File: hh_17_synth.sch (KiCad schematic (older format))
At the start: 22 parts

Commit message: switch to 48 pin chip, add headphone jack etc.
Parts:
- removed C?: 100nF, symbol C_Small
- removed U?: STM32F072RxTx, LQFP64, symbol STM32F072RxTx
- added C5, C6: 1uF, symbol C
- added C7, C8: 0.1uF, symbol C
- added J3: JACK_TRS, custom:Tayda_3.5mm_stereo_TRS_jack_A-853, symbol JACK_TRS
- added R2, R3: 8, symbol R
- added U2: STM32F072CBTx, Housings_QFP:LQFP-48_7x7mm_Pitch0.5mm, symbol STM32F072CBTx
- J1: renamed from J?; footprint (none) -> custom:HDMI_476420001_CONN
- J2: renamed from J?; footprint (none) -> Pin_Headers:Pin_Header_Straight_1x05_Pitch2.54mm
- SW1: renamed from SW?; footprint (none) -> Buttons_Switches_ThroughHole:SW_PUSH_6mm
- U1: renamed from U?; footprint (none) -> TO_SOT_Packages_SMD:SOT-223
- gave numbers to parts that had none: 16
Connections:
- wire segments 84 -> 97
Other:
- note added: "http://www.taydaelectronics.com/review/product/list/id/2876/"
- moved on the sheet: C1, C10, C12, C13, C14, C15, C16, C17, C18, C2, C3, C4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

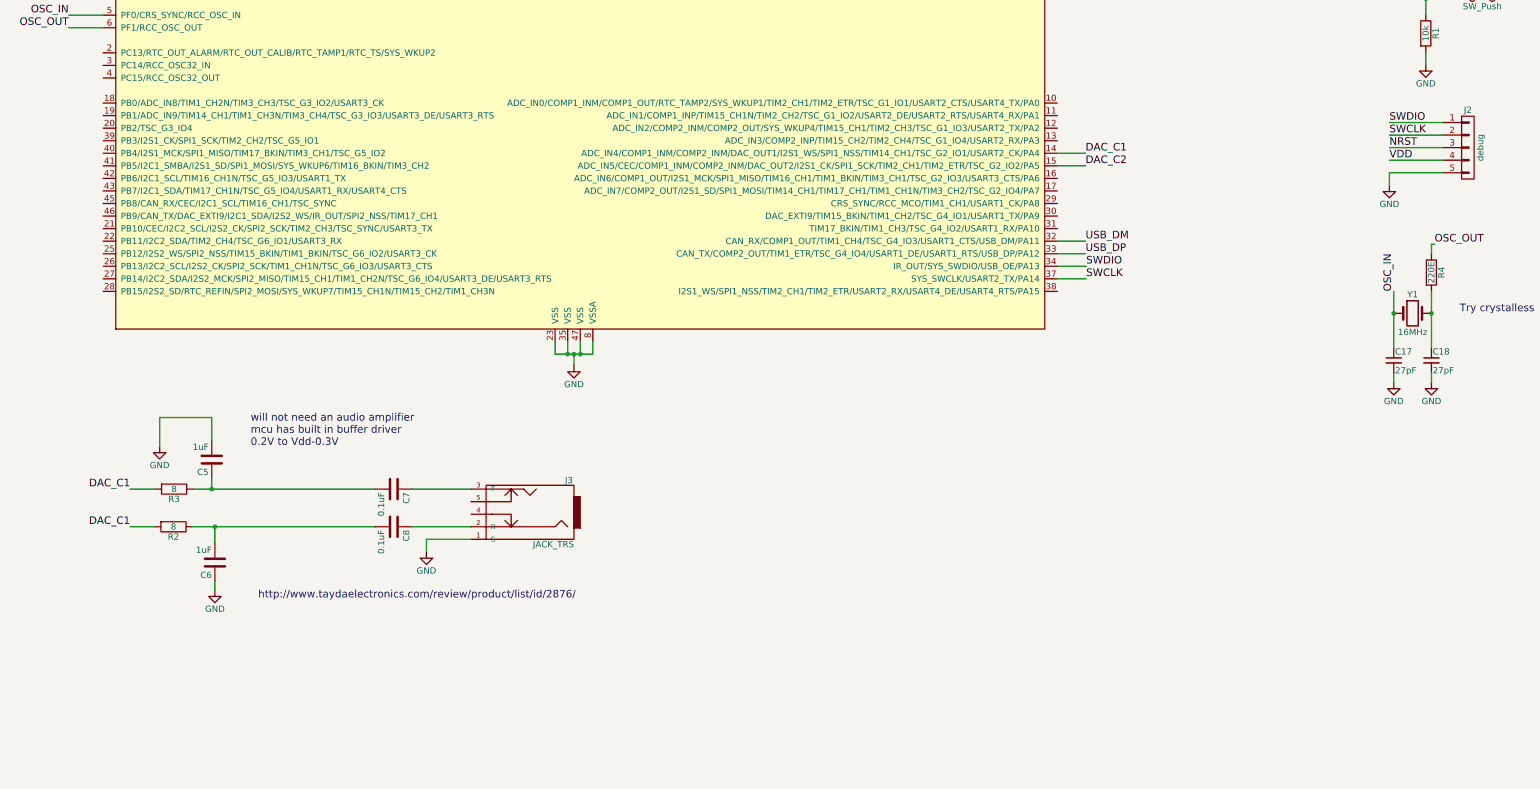
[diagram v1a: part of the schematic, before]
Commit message: Imported Mitch's touchpad and keyboard lib/mod
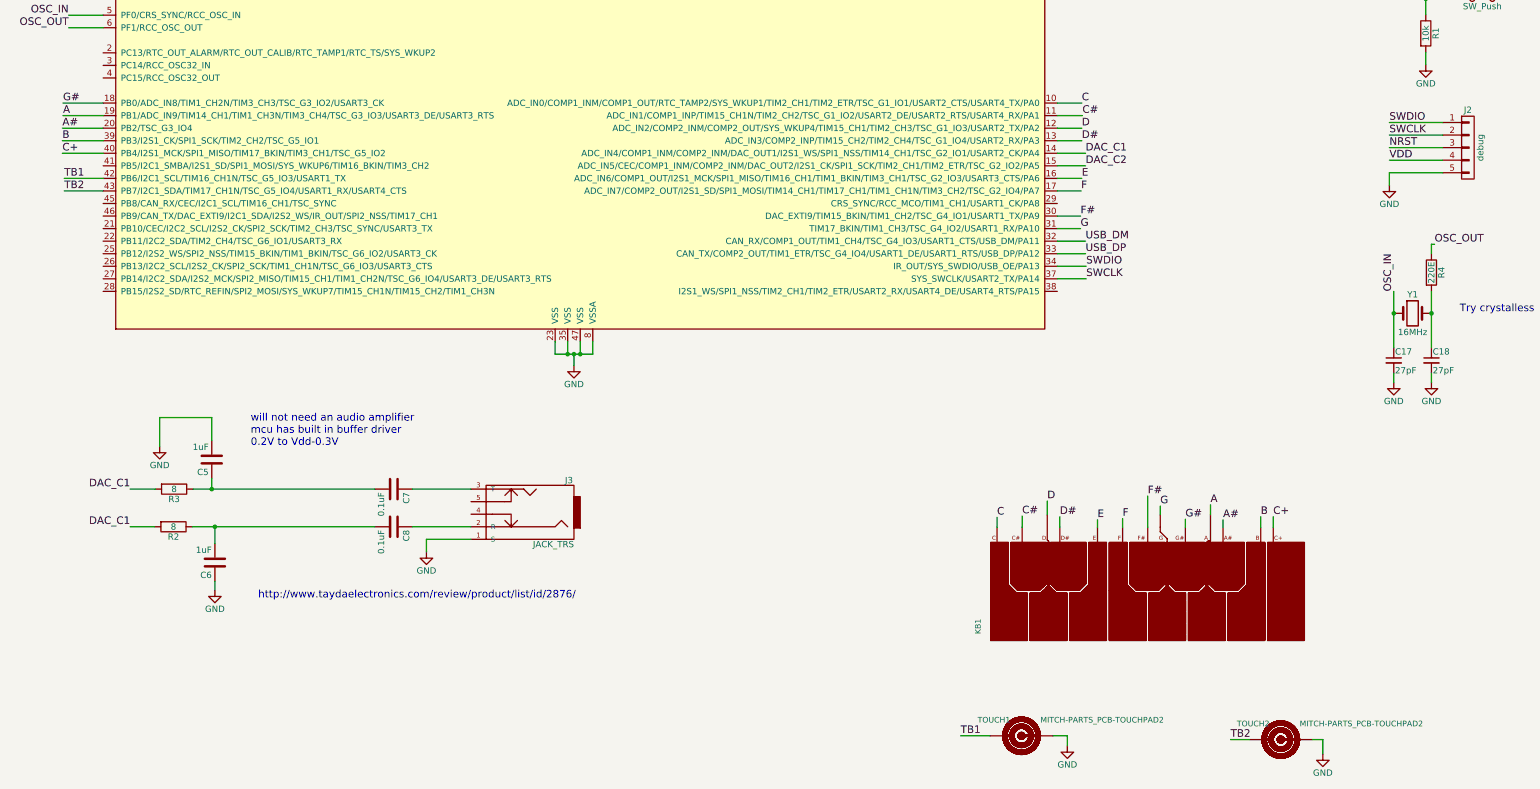
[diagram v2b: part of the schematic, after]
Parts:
- added KB1: MITCH-PARTS_PCB-KEYBOARD2, custom:MITCH-PARTS_PCB-KEYBOARD2_kicad_fix, symbol MITCH-PARTS_PCB-KEYBOARD2
- added TOUCH1, TOUCH2: MITCH-PARTS_PCB-TOUCHPAD2, custom:MITCH-PARTS_PCB-TOUCHPAD2_kicad_fix, symbol MITCH-PARTS_PCB-TOUCHPAD2
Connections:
- net GND: now also TOUCH1.2, TOUCH2.2
- net C: now reaches U2.10 (ADC_IN0/COMP1_INM/COMP1_OUT/RTC_TAMP2/SYS_WKUP1/TIM2_CH1/TIM2_ETR/TSC_G1_IO1/USART2_CTS/USART4_TX/PA0)
- net C: now also KB1.C
- net C#: now reaches U2.11 (ADC_IN1/COMP1_INP/TIM15_CH1N/TIM2_CH2/TSC_G1_IO2/USART2_DE/USART2_RTS/USART4_RX/PA1)
- net C#: now also KB1.C#
- net D: now reaches U2.12 (ADC_IN2/COMP2_INM/COMP2_OUT/SYS_WKUP4/TIM15_CH1/TIM2_CH3/TSC_G1_IO3/USART2_TX/PA2)
- net D: now also KB1.D
- net D#: now reaches U2.13 (ADC_IN3/COMP2_INP/TIM15_CH2/TIM2_CH4/TSC_G1_IO4/USART2_RX/PA3)
- net D#: now also KB1.D#
- net E: now reaches U2.16 (ADC_IN6/COMP1_OUT/I2S1_MCK/SPI1_MISO/TIM16_CH1/TIM1_BKIN/TIM3_CH1/TSC_G2_IO3/USART3_CTS/PA6)
- net E: now also KB1.E
- net F: now reaches U2.17 (ADC_IN7/COMP2_OUT/I2S1_SD/SPI1_MOSI/TIM14_CH1/TIM17_CH1/TIM1_CH1N/TIM3_CH2/TSC_G2_IO4/PA7)
- net F: now also KB1.F
- net G#: now reaches U2.18 (PB0/ADC_IN8/TIM1_CH2N/TIM3_CH3/TSC_G3_IO2/USART3_CK)
- net G#: now also KB1.G#
- net A: now reaches U2.19 (PB1/ADC_IN9/TIM14_CH1/TIM1_CH3N/TIM3_CH4/TSC_G3_IO3/USART3_DE/USART3_RTS)
- net A: now also KB1.A
- net A#: now reaches U2.20 (PB2/TSC_G3_IO4)
- net A#: now also KB1.A#
- net F#: now reaches U2.30 (DAC_EXTI9/TIM15_BKIN/TIM1_CH2/TSC_G4_IO1/USART1_TX/PA9)
- net F#: now also KB1.F#
- net G: now reaches U2.31 (TIM17_BKIN/TIM1_CH3/TSC_G4_IO2/USART1_RX/PA10)
- net G: now also KB1.G
- net B: now reaches U2.39 (PB3/I2S1_CK/SPI1_SCK/TIM2_CH2/TSC_G5_IO1)
- net B: now also KB1.B
- net C+: now reaches U2.40 (PB4/I2S1_MCK/SPI1_MISO/TIM17_BKIN/TIM3_CH1/TSC_G5_IO2)
- net C+: now also KB1.C+
- net TB1: now reaches U2.42 (PB6/I2C1_SCL/TIM16_CH1N/TSC_G5_IO3/USART1_TX)
- net TB1: now also TOUCH1.1
- net TB2: now reaches U2.43 (PB7/I2C1_SDA/TIM17_CH1N/TSC_G5_IO4/USART1_RX/USART4_CTS)
- net TB2: now also TOUCH2.1
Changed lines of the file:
@@
 LIBS:zetex
 LIBS:JACK_TRS
+LIBS:ArduTouch_stereo_v1.2
+LIBS:mitch_exported
 LIBS:hh_17_synth-cache
 EELAYER 25 0
@@
 Wire Wire Line
 	11715 5185 11485 5185
+$Comp
+L MITCH-PARTS_PCB-KEYBOARD2 KB1
+U 1 1 58A88168
+P 12205 7665
+F 0 "KB1" V 10880 7315 45  0000 L BNN
+F 1 "MITCH-PARTS_PCB-KEYBOARD2" V 12205 7665 45  0001 L BNN
+F 2 "custom:MITCH-PARTS_PCB-KEYBOARD2_kicad_fix" H 12235 7815 20  0001 C CNN
+F 3 "" H 12205 7665 60  0001 C CNN
+	1    12205 7665
+	1    0    0    -1
+$EndComp
+$Comp
+L MITCH-PARTS_PCB-TOUCHPAD2 TOUCH1
+U 1 1 58A8CBB1
+P 11200 8825
+F 0 "TOUCH1" H 10850 8925 45  0000 L BNN
+F 1 "MITCH-PARTS_PCB-TOUCHPAD2" H 11350 8925 45  0000 L BNN
+F 2 "custom:MITCH-PARTS_PCB-TOUCHPAD2_kicad_fix" H 11230 8975 20  0001 C CNN
+F 3 "" H 11200 8825 60  0001 C CNN
+	1    11200 8825
+	1    0    0    -1
+$EndComp
+$Comp
+L MITCH-PARTS_PCB-TOUCHPAD2 TOUCH2
+U 1 1 58A8CCDE
+P 13265 8855
+F 0 "TOUCH2" H 12915 8955 45  0000 L BNN
+F 1 "MITCH-PARTS_PCB-TOUCHPAD2" H 13415 8955 45  0000 L BNN
+F 2 "custom:MITCH-PARTS_PCB-TOUCHPAD2_kicad_fix" H 13295 9005 20  0001 C CNN
+F 3 "" H 13265 8855 60  0001 C CNN
+	1    13265 8855
+	1    0    0    -1
+$EndComp
+Text Label 11680 3785 0    60   ~ 0
+C
+Text Label 11685 3885 0    60   ~ 0
+C#
+Text Label 11680 3985 0    60   ~ 0
+D
+Text Label 11680 4085 0    60   ~ 0
+D#
+Wire Wire Line
+	11485 4085 11680 4085
+Wire Wire Line
+	11680 3985 11485 3985
+Wire Wire Line
+	11485 3885 11685 3885
+Wire Wire Line
+	11680 3785 11485 3785
+Text Label 11005 7085 0    60   ~ 0
+C
+Wire Wire Line
+	11005 7085 11005 7165
+Text Label 11205 7075 0    60   ~ 0
+C#
+Wire Wire Line
+	11205 7075 11205 7165
+Text Label 11405 6955 0    60   ~ 0
+D
+Wire Wire Line
+	11405 6955 11405 7065
+Text Label 11505 7080 0    60   ~ 0
+D#
+Wire Wire Line
+	11505 7080 11505 7165
+Text Label 11680 4385 0    60   ~ 0
+E
+Text Label 11675 4485 0    60   ~ 0
+F
+Wire Wire Line
+	11675 4485 11485 4485
+Wire Wire Line
+	11680 4385 11485 4385
+Text Label 11805 7105 0    60   ~ 0
+E
+Wire Wire Line
+	11805 7105 11805 7165
+Text Label 12005 7095 0    60   ~ 0
+F
+Wire Wire Line
+	12005 7095 12005 7165
+Text Label 11670 4685 0    60   ~ 0
+F#
+Wire Wire Line
+	11670 4685 11485 4685
+Text Label 11670 4785 0    60   ~ 0
+G
+Wire Wire Line
+	11670 4785 11485 4785
+Text Label 12205 6915 0    60   ~ 0
+F#
+Wire Wire Line
+	12205 6915 12205 7165
+Text Label 12305 6995 0    60   ~ 0
+G
+Wire Wire Line
+	12305 6995 12305 7065
+Text Label 3565 3785 0    60   ~ 0
+G#
+Text Label 3565 3885 0    60   ~ 0
+A
+Text Label 3560 3985 0    60   ~ 0
+A#
+Wire Wire Line
+	3560 3985 3885 3985
+Wire Wire Line
+	3885 3885 3565 3885
+Wire Wire Line
+	3565 3785 3885 3785
+Text Label 12505 7100 0    60   ~ 0
+G#
+Wire Wire Line
+	12505 7100 12505 7165
+Text Label 12705 6985 0    60   ~ 0
+A
+Wire Wire Line
+	12705 6985 12705 7065
+Text Label 12805 7105 0    60   ~ 0
+A#
+Wire Wire Line
+	12805 7105 12805 7165
+Text Label 13105 7080 0    60   ~ 0
+B
+Text Label 13205 7080 0    60   ~ 0
+C+
+Wire Wire Line
+	13105 7080 13105 7165
+Wire Wire Line
+	13205 7165 13205 7080
+Text Label 3560 4085 0    60   ~ 0
+B
+Text Label 3560 4185 0    60   ~ 0
+C+
+Wire Wire Line
+	3560 4185 3885 4185
+Wire Wire Line
+	3885 4085 3560 4085
+$Comp
+L GND #PWR015
+U 1 1 58A9B332
+P 11565 8905
+F 0 "#PWR015" H 11565 8655 50  0001 C CNN
+F 1 "GND" H 11565 8755 50  0000 C CNN
+F 2 "" H 11565 8905 50  0001 C CNN
+F 3 "" H 11565 8905 50  0001 C CNN
+	1    11565 8905
+	1    0    0    -1
+$EndComp
+Wire Wire Line
+	11450 8825 11565 8825
+Wire Wire Line
+	11565 8825 11565 8905
+$Comp
+L GND #PWR016
+U 1 1 58A9B570
+P 13600 8970
+F 0 "#PWR016" H 13600 8720 50  0001 C CNN
+F 1 "GND" H 13600 8820 50  0000 C CNN
+F 2 "" H 13600 8970 50  0001 C CNN
+F 3 "" H 13600 8970 50  0001 C CNN
+	1    13600 8970
+	1    0    0    -1
+$EndComp
+Wire Wire Line
+	13600 8970 13600 8855
+Wire Wire Line
+	13600 8855 13515 8855
+Text Label 3575 4385 0    60   ~ 0
+TB1
+Text Label 3575 4485 0    60   ~ 0
+TB2
+Wire Wire Line
+	3575 4485 3885 4485
+Wire Wire Line
+	3575 4385 3885 4385
+Text Label 10715 8825 0    60   ~ 0
+TB1
+Wire Wire Line
+	10715 8825 10950 8825
+Text Label 12865 8855 0    60   ~ 0
+TB2
+Wire Wire Line
+	13015 8855 12865 8855
 $EndSCHEMATC

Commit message: placed parts, changed some footprints.
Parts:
- removed C6: 1uF, symbol C
- added C6: 1uF, Capacitors_ThroughHole:CP_Radial_D5.0mm_P2.00mm, symbol CP1
- C1: value C -> 1uF; footprint (none) -> Capacitors_SMD:C_0603
- C10, C12, C13, C14, C15, C16, C17, C18, C2, C3, C4, C7, C8, C9: footprint (none) -> Capacitors_SMD:C_0603
- C5: footprint (none) -> Capacitors_ThroughHole:CP_Radial_D5.0mm_P2.00mm; symbol C -> CP1; Manufacturer (none) -> Cornell Dubilier; Mfg_Part_No (none) -> 105CKR050M
- R1, R2, R3, R4: footprint (none) -> Resistors_SMD:R_0603
- Y1: footprint (none) -> Crystals:Crystal_HC49-4H_Vertical
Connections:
- net DAC_C1: no longer R2.2
- net DAC_C2: now also R2.2
- net GND: now also C6.2
- net at C8.2, R2.1: now also C6.1
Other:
- note added: "TODO: choose button and verify button footprint"
- note added: "TODO: verify load capacitance, fix crystal"
- note added: "TODO: verify lpf"
- note removed: "Try crystalless"
- moved on the sheet: R2, R3
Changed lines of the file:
@@
 LIBS:JACK_TRS
 LIBS:ArduTouch_stereo_v1.2
-LIBS:mitch_exported
 LIBS:hh_17_synth-cache
 EELAYER 25 0
@@
 F 0 "Y1" H 14315 5610 50  0000 C CNN
 F 1 "16MHz" H 14315 5310 50  0000 C CNN
-F 2 "" H 14315 5460 50  0001 C CNN
+F 2 "Crystals:Crystal_HC49-4H_Vertical" H 14315 5460 50  0001 C CNN
 F 3 "" H 14315 5460 50  0000 C CNN
 	1    14315 5460
@@
 F 0 "R4" V 14545 5135 50  0000 C CNN
 F 1 "220E" V 14465 5135 50  0000 C CNN
-F 2 "" V 14395 5135 50  0001 C CNN
+F 2 "Resistors_SMD:R_0603" V 14395 5135 50  0001 C CNN
 F 3 "" H 14465 5135 50  0000 C CNN
 	1    14465 5135
@@
 F 0 "C17" H 14175 5905 50  0000 L CNN
 F 1 "27pF" H 14175 5755 50  0000 L CNN
-F 2 "" H 14165 5835 50  0001 C CNN
+F 2 "Capacitors_SMD:C_0603" H 14165 5835 50  0001 C CNN
 F 3 "" H 14165 5835 50  0000 C CNN
 	1    14165 5835
@@
 F 0 "C18" H 14475 5905 50  0000 L CNN
 F 1 "27pF" H 14475 5755 50  0000 L CNN
-F 2 "" H 14465 5835 50  0001 C CNN
+F 2 "Capacitors_SMD:C_0603" H 14465 5835 50  0001 C CNN
 F 3 "" H 14465 5835 50  0000 C CNN
 	1    14465 5835
@@
 F 0 "C12" H 7865 1220 50  0000 L CNN
 F 1 "100nF" V 7855 750 50  0000 L CNN
-F 2 "" H 7855 1150 50  0001 C CNN
+F 2 "Capacitors_SMD:C_0603" H 7855 1150 50  0001 C CNN
 F 3 "" H 7855 1150 50  0000 C CNN
 	1    7855 1150
@@
 F 0 "C13" H 7865 1395 50  0000 L CNN
 F 1 "100nF" V 7855 925 50  0000 L CNN
-F 2 "" H 7855 1325 50  0001 C CNN
+F 2 "Capacitors_SMD:C_0603" H 7855 1325 50  0001 C CNN
 F 3 "" H 7855 1325 50  0000 C CNN
 	1    7855 1325
@@
 F 0 "C14" H 7865 1570 50  0000 L CNN
 F 1 "4.7uF" V 7855 1100 50  0000 L CNN
-F 2 "" H 7855 1500 50  0001 C CNN
+F 2 "Capacitors_SMD:C_0603" H 7855 1500 50  0001 C CNN
 F 3 "" H 7855 1500 50  0000 C CNN
 	1    7855 1500
@@
 F 0 "C16" H 8490 1570 50  0000 L CNN
 F 1 "10nF" V 8480 1100 50  0000 L CNN
-F 2 "" H 8480 1500 50  0001 C CNN
+F 2 "Capacitors_SMD:C_0603" H 8480 1500 50  0001 C CNN
 F 3 "" H 8480 1500 50  0000 C CNN
 	1    8480 1500
@@
 F 0 "C15" H 8490 1395 50  0000 L CNN
 F 1 "1uF" V 8480 925 50  0000 L CNN
-F 2 "" H 8480 1325 50  0001 C CNN
+F 2 "Capacitors_SMD:C_0603" H 8480 1325 50  0001 C CNN
 F 3 "" H 8480 1325 50  0000 C CNN
 	1    8480 1325
@@
 F 0 "C9" H 9200 1740 50  0000 L CNN
 F 1 "100nF" V 9240 1370 50  0000 L CNN
-F 2 "" H 9190 1670 50  0001 C CNN
+F 2 "Capacitors_SMD:C_0603" H 9190 1670 50  0001 C CNN
 F 3 "" H 9190 1670 50  0000 C CNN
 	1    9190 1670
@@
 F 0 "C10" H 9200 1940 50  0000 L CNN
 F 1 "4.7uF" V 9240 1595 50  0000 L CNN
-F 2 "" H 9190 1870 50  0001 C CNN
+F 2 "Capacitors_SMD:C_0603" H 9190 1870 50  0001 C CNN
 F 3 "" H 9190 1870 50  0000 C CNN
 	1    9190 1870
@@
 F 0 "C2" V 13115 790 50  0000 L CNN
 F 1 "1uF" V 13065 1165 50  0000 L CNN
-F 2 "" H 13065 940 50  0001 C CNN
+F 2 "Capacitors_SMD:C_0603" H 13065 940 50  0001 C CNN
 F 3 "" H 13065 940 50  0000 C CNN
 	1    13065 940
@@
 F 0 "C3" V 13115 965 50  0000 L CNN
 F 1 "100nF" V 13015 1340 50  0000 L CNN
-F 2 "" H 13065 1115 50  0001 C CNN
+F 2 "Capacitors_SMD:C_0603" H 13065 1115 50  0001 C CNN
 F 3 "" H 13065 1115 50  0000 C CNN
 	1    13065 1115
@@
 F 0 "C4" V 13115 1140 50  0000 L CNN
 F 1 "10nF" V 13065 1515 50  0000 L CNN
-F 2 "" H 13065 1290 50  0001 C CNN
+F 2 "Capacitors_SMD:C_0603" H 13065 1290 50  0001 C CNN
 F 3 "" H 13065 1290 50  0000 C CNN
 	1    13065 1290
@@
 Text Label 11710 4985 0    60   ~ 0
 USB_DP
-Text Notes 14690 5460 0    60   ~ 0
-Try crystalless
 $Comp
 L LM1117-3.3 U1
@@
 P 15145 1650
 F 0 "C1" H 15170 1750 50  0000 L CNN
-F 1 "C" H 15170 1550 50  0000 L CNN
-F 2 "" H 15183 1500 50  0001 C CNN
+F 1 "1uF" H 15170 1550 50  0000 L CNN
+F 2 "Capacitors_SMD:C_0603" H 15183 1500 50  0001 C CNN
 F 3 "" H 15145 1650 50  0001 C CNN
 	1    15145 1650
@@
 F 0 "R1" V 14500 3230 50  0000 C CNN
 F 1 "10k" V 14420 3230 50  0000 C CNN
-F 2 "" V 14350 3230 50  0001 C CNN
+F 2 "Resistors_SMD:R_0603" V 14350 3230 50  0001 C CNN
 F 3 "" H 14420 3230 50  0001 C CNN
 	1    14420 3230
@@
 	-1   0    0    1
 $EndComp
-Text Notes 5120 7740 0    60   ~ 0
+Text Notes 5790 8090 0    60   ~ 0
 http://www.taydaelectronics.com/review/product/list/id/2876/
 $Comp
@@
 	1    0    0    -1
 $EndComp
-Text Label 4100 7160 2    60   ~ 0
-DAC_C1
-Text Label 4100 6860 2    60   ~ 0
+Text Label 3530 7535 2    60   ~ 0
+DAC_C2
+Text Label 3555 6860 2    60   ~ 0
 DAC_C1
 $Comp
@@
 F 0 "C8" H 6225 7260 50  0000 L CNN
 F 1 "0.1uF" H 6225 7060 50  0000 L CNN
-F 2 "" H 6238 7010 50  0001 C CNN
+F 2 "Capacitors_SMD:C_0603" H 6238 7010 50  0001 C CNN
 F 3 "" H 6200 7160 50  0001 C CNN
 	1    6200 7160
@@
 F 0 "C7" H 6225 6960 50  0000 L CNN
 F 1 "0.1uF" H 6225 6760 50  0000 L CNN
-F 2 "" H 6238 6710 50  0001 C CNN
+F 2 "Capacitors_SMD:C_0603" H 6238 6710 50  0001 C CNN
 F 3 "" H 6200 6860 50  0001 C CNN
 	1    6200 6860
@@
 $EndComp
 $Comp
-L C C5
+L CP1 C5
 U 1 1 58A72315
-P 4750 6625
-F 0 "C5" H 4775 6725 50  0000 L CNN
-F 1 "1uF" H 4775 6525 50  0000 L CNN
-F 2 "" H 4788 6475 50  0001 C CNN
-F 3 "" H 4750 6625 50  0001 C CNN
-	1    4750 6625
-	-1   0    0    1
-$EndComp
-$Comp
-L C C6
-U 1 1 58A7240F
-P 4775 7445
-F 0 "C6" H 4800 7545 50  0000 L CNN
-F 1 "1uF" H 4800 7345 50  0000 L CNN
-F 2 "" H 4813 7295 50  0001 C CNN
-F 3 "" H 4775 7445 50  0001 C CNN
-	1    4775 7445
-	-1   0    0    1
+P 4205 7095
+F 0 "C5" H 4230 7195 50  0000 L CNN
+F 1 "1uF" H 4230 6995 50  0000 L CNN
+F 2 "Capacitors_ThroughHole:CP_Radial_D5.0mm_P2.00mm" H 4243 6945 50  0001 C CNN
+F 3 "" H 4205 7095 50  0001 C CNN
+F 4 "105CKR050M" H 4205 7095 60  0001 C CNN "Mfg_Part_No"
+F 5 "Cornell Dubilier" H 4205 7095 60  0001 C CNN "Manufacturer"
+	1    4205 7095
+	1    0    0    -1
 $EndComp
 $Comp
 L GND #PWR012
 U 1 1 58A724D3
-P 4335 6520
-F 0 "#PWR012" H 4335 6270 50  0001 C CNN
-F 1 "GND" H 4335 6370 50  0000 C CNN
-F 2 "" H 4335 6520 50  0001 C CNN
-F 3 "" H 4335 6520 50  0001 C CNN
-	1    4335 6520
+P 4205 7320
+F 0 "#PWR012" H 4205 7070 50  0001 C CNN
+F 1 "GND" H 4205 7170 50  0000 C CNN
+F 2 "" H 4205 7320 50  0001 C CNN
+F 3 "" H 4205 7320 50  0001 C CNN
+	1    4205 7320
 	1    0    0    -1
 $EndComp
@@
 L GND #PWR013
 U 1 1 58A72C41
-P 4775 7665
-F 0 "#PWR013" H 4775 7415 50  0001 C CNN
-F 1 "GND" H 4775 7515 50  0000 C CNN
-F 2 "" H 4775 7665 50  0001 C CNN
-F 3 "" H 4775 7665 50  0001 C CNN
-	1    4775 7665
+P 4205 8040
+F 0 "#PWR013" H 4205 7790 50  0001 C CNN
+F 1 "GND" H 4205 7890 50  0000 C CNN
+F 2 "" H 4205 8040 50  0001 C CNN
+F 3 "" H 4205 8040 50  0001 C CNN
+	1    4205 8040
 	1    0    0    -1
 $EndComp
@@
 L R R3
 U 1 1 58A73023
-P 4450 6860
-F 0 "R3" V 4530 6860 50  0000 C CNN
-F 1 "8" V 4450 6860 50  0000 C CNN
-F 2 "" V 4380 6860 50  0001 C CNN
-F 3 "" H 4450 6860 50  0001 C CNN
-	1    4450 6860
+P 3905 6860
+F 0 "R3" V 3985 6860 50  0000 C CNN
+F 1 "8" V 3905 6860 50  0000 C CNN
+F 2 "Resistors_SMD:R_0603" V 3835 6860 50  0001 C CNN
+F 3 "" H 3905 6860 50  0001 C CNN
+	1    3905 6860
 	0    1    1    0
 $EndComp
@@
 L R R2
 U 1 1 58A73182
-P 4445 7160
-F 0 "R2" V 4525 7160 50  0000 C CNN
-F 1 "8" V 4445 7160 50  0000 C CNN
-F 2 "" V 4375 7160 50  0001 C CNN
-F 3 "" H 4445 7160 50  0001 C CNN
-	1    4445 7160
+P 3875 7535
+F 0 "R2" V 3955 7535 50  0000 C CNN
+F 1 "8" V 3875 7535 50  0000 C CNN
+F 2 "Resistors_SMD:R_0603" V 3805 7535 50  0001 C CNN
+F 3 "" H 3875 7535 50  0001 C CNN
+	1    3875 7535
 	0    1    1    0
 $EndComp
@@
 Wire Wire Line
 	3420 2685 3885 2685
-Connection ~ 4750 6860
-Wire Wire Line
-	4750 6775 4750 6860
-Connection ~ 4775 7160
-Wire Wire Line
-	4775 7295 4775 7160
-Wire Wire Line
-	4595 7160 6050 7160
-Wire Wire Line
-	4600 6860 6050 6860
-Wire Wire Line
-	4100 6860 4300 6860
-Wire Wire Line
-	4295 7160 4100 7160
-Wire Wire Line
-	4775 7665 4775 7595
-Wire Wire Line
-	4750 6290 4750 6475
-Wire Wire Line
-	4335 6290 4750 6290
-Wire Wire Line
-	4335 6520 4335 6290
+Connection ~ 4205 7535
+Wire Wire Line
+	4205 7670 4205 7535
+Wire Wire Line
+	4025 7535 5765 7535
+Wire Wire Line
+	4055 6860 6050 6860
+Wire Wire Line
+	3555 6860 3755 6860
+Wire Wire Line
+	3725 7535 3530 7535
+Wire Wire Line
+	4205 8040 4205 7970
 Wire Wire Line
 	6350 7160 6815 7160
@@
 Wire Wire Line
 	13015 8855 12865 8855
+Wire Wire Line
+	6050 7160 5765 7160
+Wire Wire Line
+	5765 7160 5765 7535
+Wire Wire Line
+	4205 7320 4205 7245
+Wire Wire Line
+	4205 6860 4205 6945
+Connection ~ 4205 6860
+$Comp
+L CP1 C6
+U 1 1 58A9EF73
+P 4205 7820
+F 0 "C6" H 4230 7920 50  0000 L CNN
+F 1 "1uF" H 4230 7720 50  0000 L CNN
+F 2 "Capacitors_ThroughHole:CP_Radial_D5.0mm_P2.00mm" H 4243 7670 50  0001 C CNN
+F 3 "" H 4205 7820 50  0001 C CNN
+F 4 "105CKR050M" H 4205 7820 60  0001 C CNN "Mfg_Part_No"
+F 5 "Cornell Dubilier" H 4205 7820 60  0001 C CNN "Manufacturer"
+	1    4205 7820
+	1    0    0    -1
+$EndComp
+Text Notes 13440 6335 0    60   ~ 0
+TODO: verify load capacitance, fix crystal
+Text Notes 3135 8480 0    60   ~ 0
+TODO: verify lpf
+Text Notes 13700 2725 0    60   ~ 0
+TODO: choose button and verify button footprint
 $EndSCHEMATC
